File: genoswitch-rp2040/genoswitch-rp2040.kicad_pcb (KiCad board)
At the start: 2 copper layers, 43.4 x 49 mm, 44 parts, among them J1 USB_B_Micro, J10 RP2040_ADC2, J11 RP2040_ADC3, J2 Conn_01x03_Socket-PicoDebug, J3 HW-SPI0, J4 HW-SPI1, J5 PIO-SPI0, J6 PIO-SPI1, J7 SERIAL, J8 RP2040_ADC0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

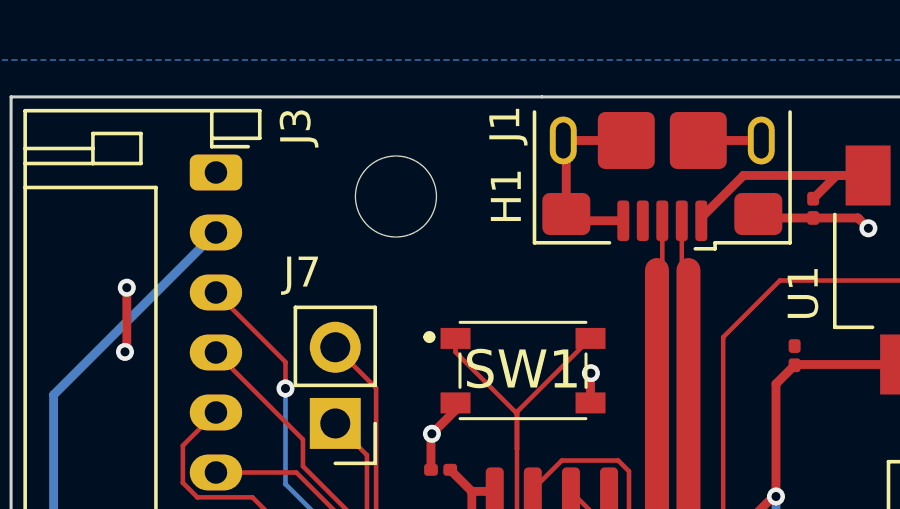
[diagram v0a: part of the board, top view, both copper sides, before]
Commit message: (debug): update pcb
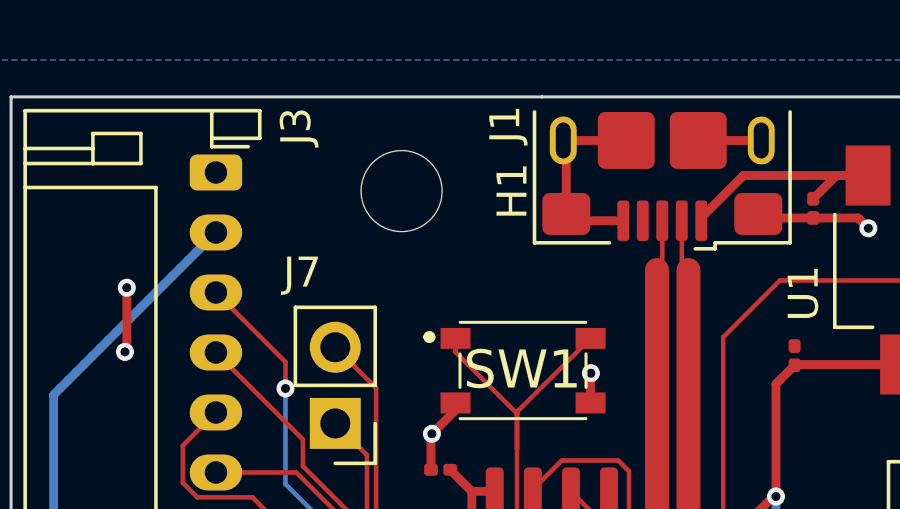
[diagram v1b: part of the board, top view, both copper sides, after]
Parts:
- moved H1 0.26 mm to (98.6, 47.4)
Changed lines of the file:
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@@
   )
   (footprint "MountingHole:MountingHole_2.7mm_M2.5" (layer "F.Cu")
-    (at 98.412 47.55 -90)
+    (at 98.6 47.37 -90)
     (descr "Mounting Hole 2.7mm, no annular, M2.5")
     (tags "mounting hole 2.7mm no annular m2.5")
